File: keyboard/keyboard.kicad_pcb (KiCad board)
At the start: 2 copper layers, 134.3 x 93.3 mm, 40 parts

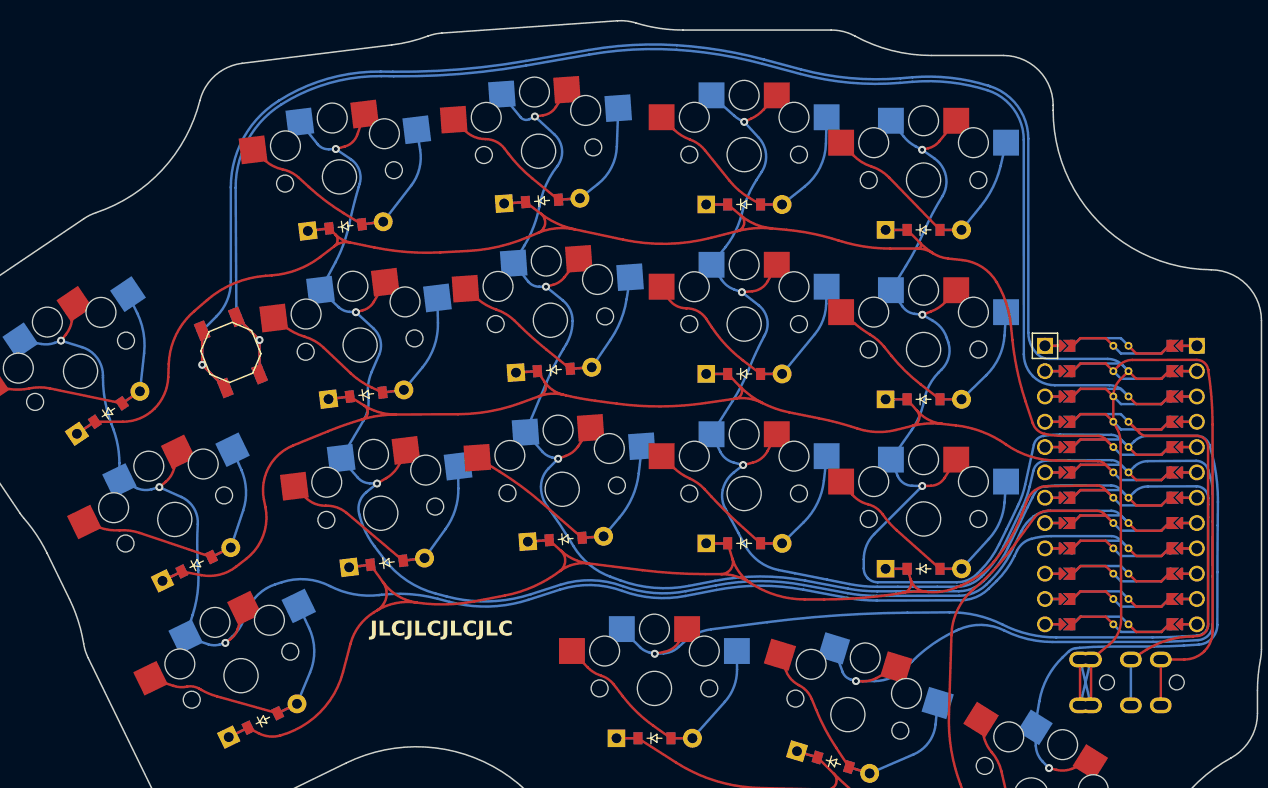
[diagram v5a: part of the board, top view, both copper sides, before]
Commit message: Re-route traces a to look more organic
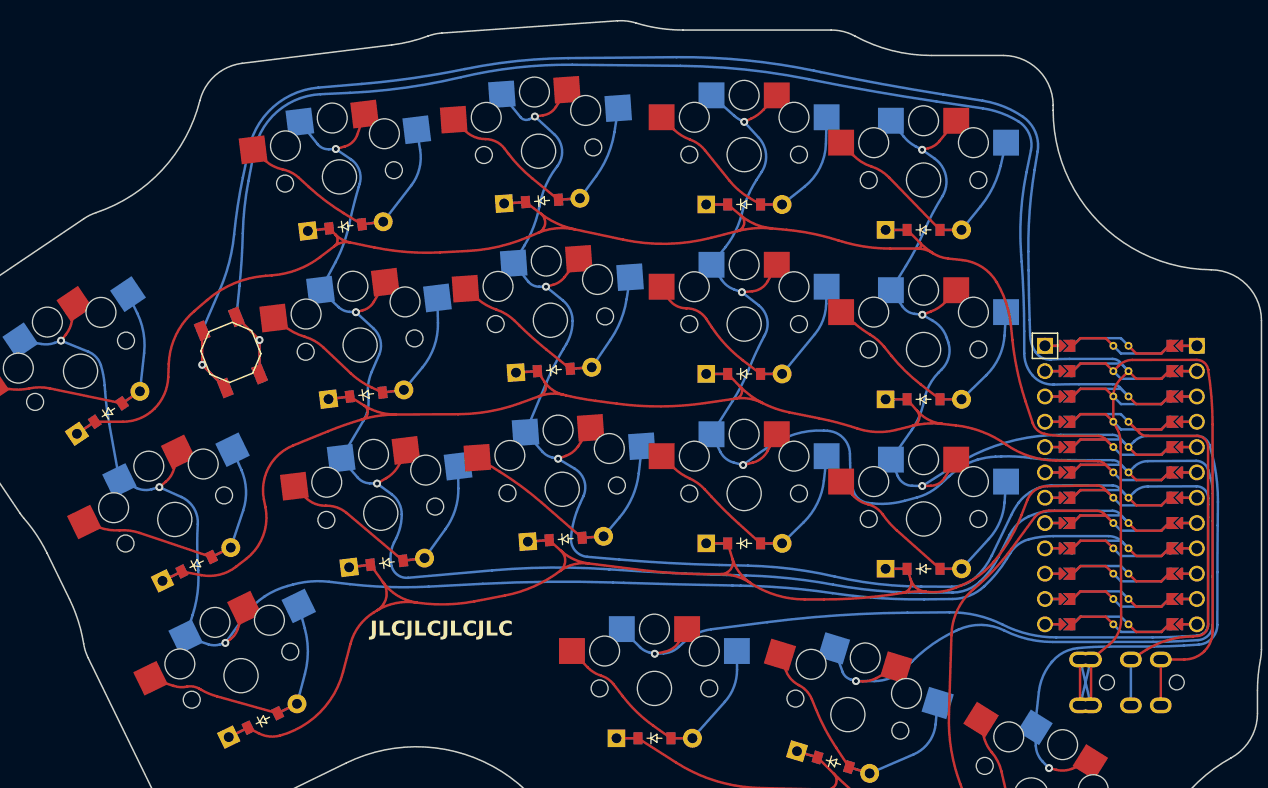
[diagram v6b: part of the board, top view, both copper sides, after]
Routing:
- net F4: track 167.1 -> 142.1 mm
- net F5: track 188.6 -> 178.2 mm
- net GND: track 199.3 -> 194.0 mm
- net RST: track 148.8 -> 143.5 mm
- net B1: track 156.4 -> 154.7 mm
- net F7: track 150.2 -> 148.5 mm
- net F6: track 221.3 -> 220.0 mm

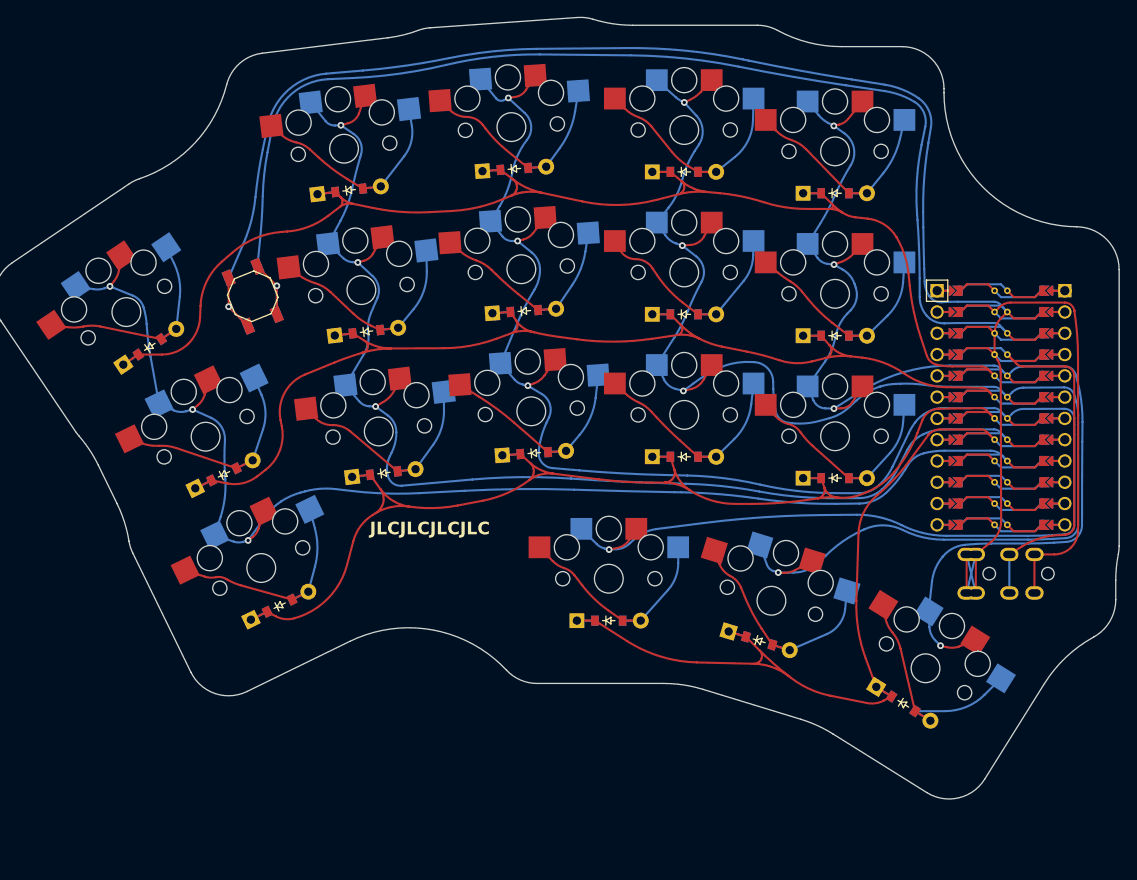
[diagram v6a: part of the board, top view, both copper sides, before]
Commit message: Add an extra thumb key (extra tucky)
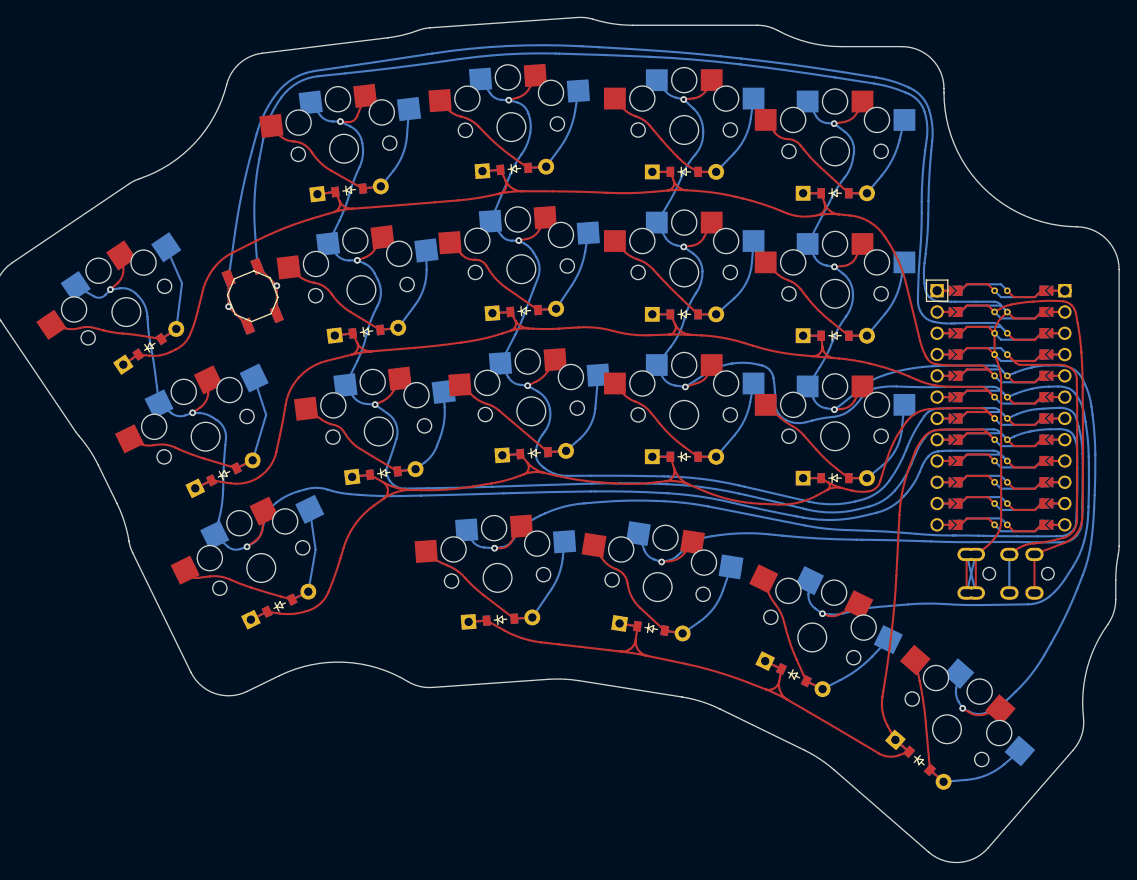
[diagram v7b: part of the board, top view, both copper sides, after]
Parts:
- added D19: , ComboDiode, F.Cu at (256.1, 158.9)
- added S19: , PG1350, F.Cu at (259.4, 155.2)
- moved S18 14.0 mm to (243.3, 144.2), turned to -26 degrees
- moved S17 13.7 mm to (224.9, 138.2), turned to -9 degrees
- moved D18 13.5 mm to (241.1, 148.7), turned to -26 degrees
- moved S16 13.3 mm to (205.8, 137.1), turned to 4 degrees
- moved D17 13.0 mm to (224.1, 143.1), turned to -9 degrees
- moved D16 12.9 mm to (206.1, 142.1), turned to 4 degrees
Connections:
- D16 pad 2: tucky_thumb -> extra_tucky_thumb
- D17 pad 2: resty_thumb -> tucky_thumb
- D18 pad 2: reachy_thumb -> resty_thumb
- S16 pad 1: F6 -> F7
- S16 pad 2: tucky_thumb -> extra_tucky_thumb
- S17 pad 1: F5 -> F6
- S17 pad 2: resty_thumb -> tucky_thumb
- S18 pad 1: F4 -> F5
- S18 pad 2: reachy_thumb -> resty_thumb
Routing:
- net F7: track 148.5 -> 249.3 mm, vias 3 -> 4
- net C6: track 101.6 -> 130.2 mm
- net extra_tucky_thumb: track 0.00 -> 26.8 mm
- net F4: track 142.1 -> 149.5 mm
- net F5: track 178.2 -> 171.0 mm
- net B1: track 154.7 -> 160.9 mm
- net RST: track 143.5 -> 148.6 mm
- net GND: track 194.0 -> 198.9 mm
- net D0: track 150.8 -> 146.1 mm
- net D1: track 169.6 -> 165.1 mm
- net D4: track 150.5 -> 146.5 mm
- net F6: track 220.0 -> 217.7 mm
- net resty_thumb: track 28.6 -> 26.4 mm
- net far_home: track 27.9 -> 26.1 mm
- net middle_home: track 26.0 -> 27.8 mm
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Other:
- board size 134.3 x 93.3 mm -> 134.3 x 100.9 mm
- board text removed: "JLCJLCJLCJLC"

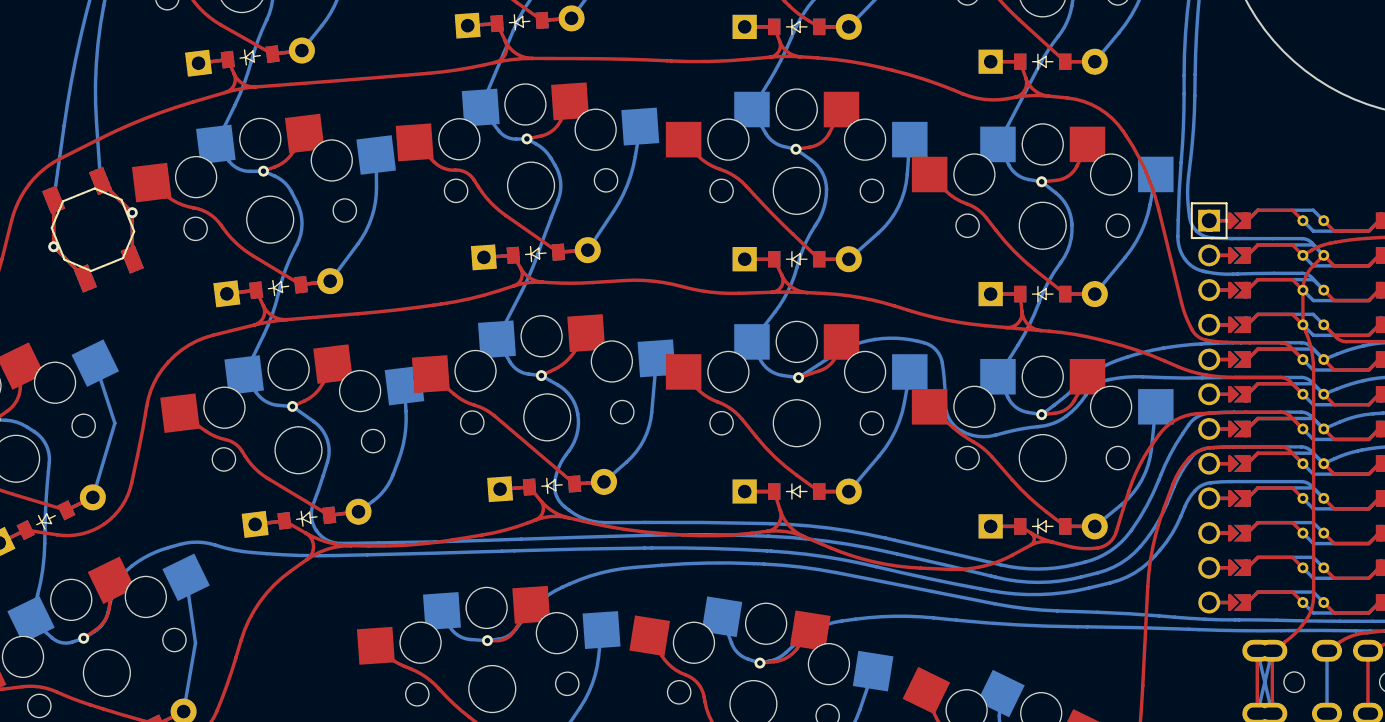
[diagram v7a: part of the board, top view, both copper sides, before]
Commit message: Fill in unfilled zone, tweak curve
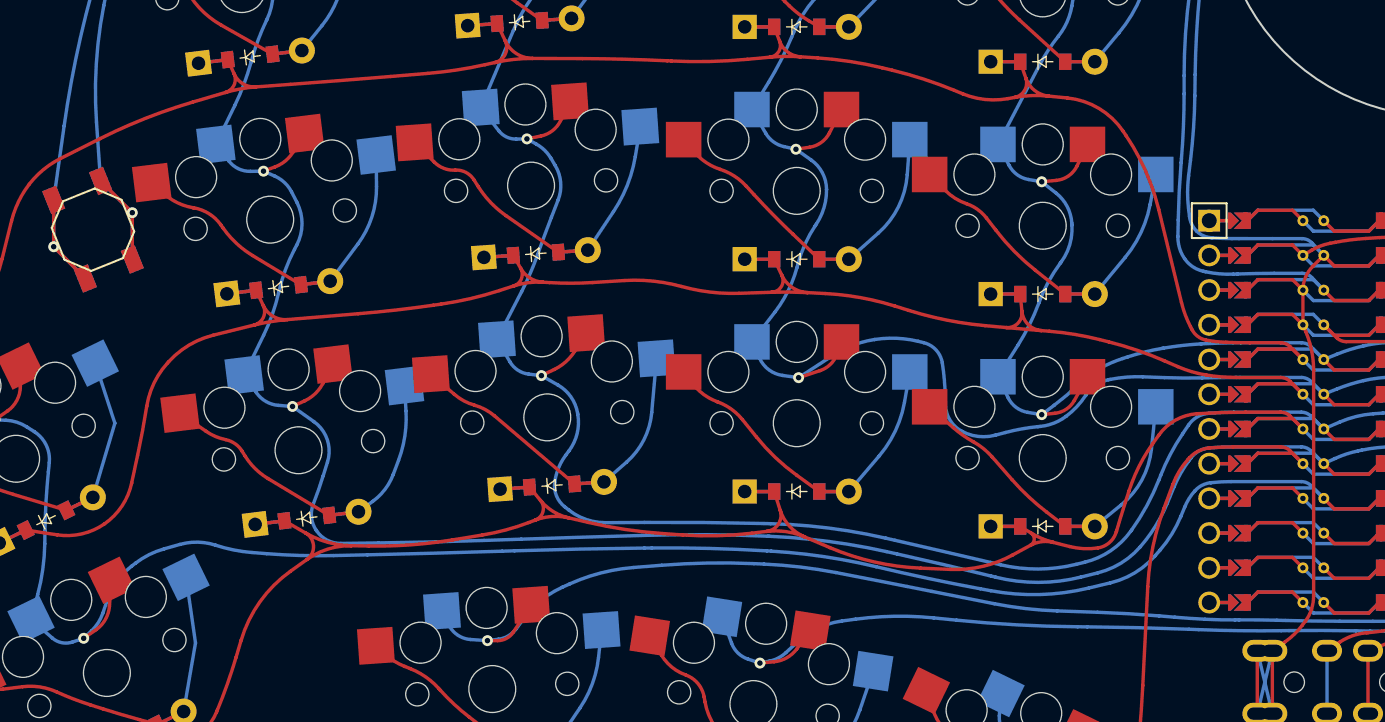
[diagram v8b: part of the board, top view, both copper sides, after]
